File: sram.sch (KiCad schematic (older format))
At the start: 4 parts, among them U1 ICE40HX4K-TQ144, U2 IS61WV5128EDBLL-10TLI

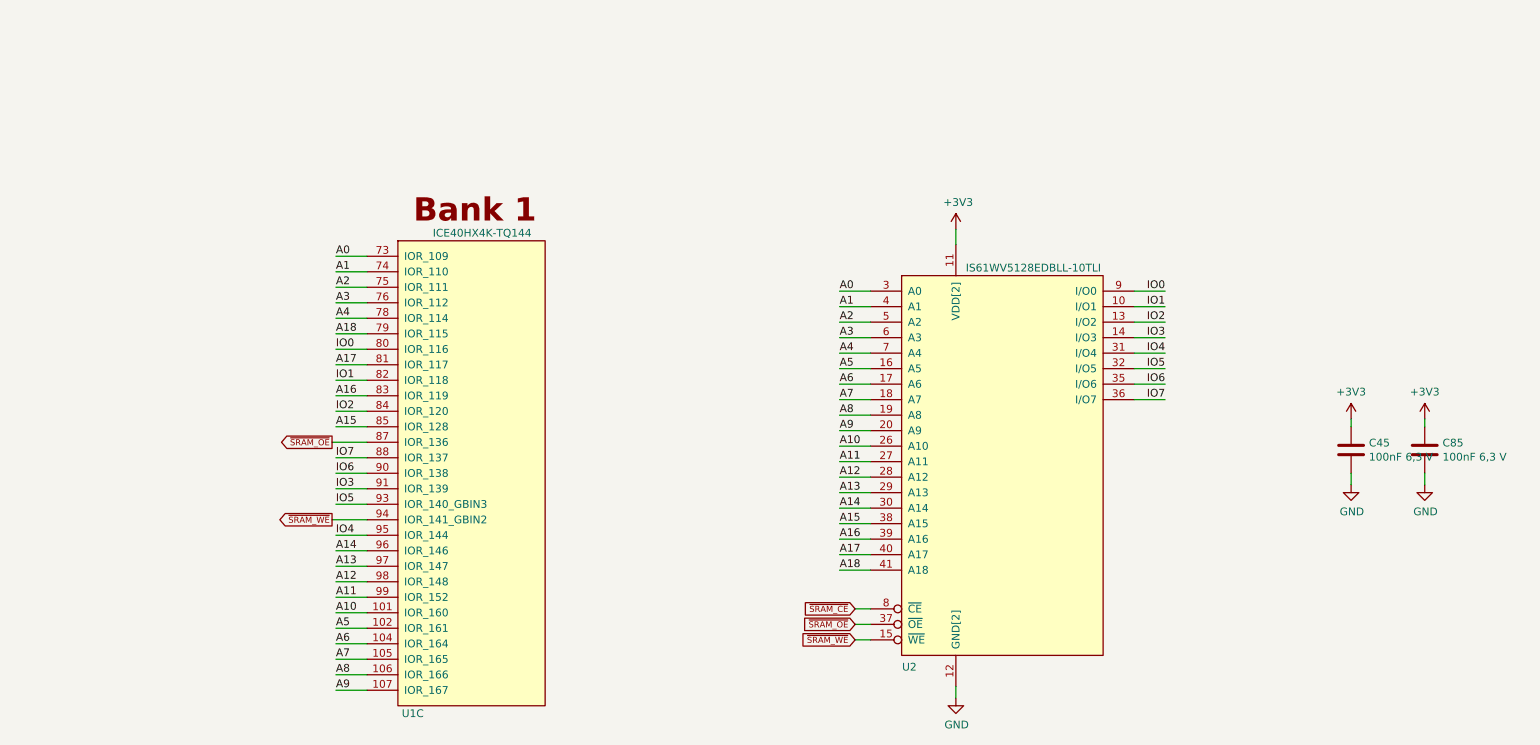
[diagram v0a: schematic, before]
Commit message: Schematic modified (Hierarchy) Bug where SPI was active when creset or ss was low fixed PCB layout started (almost all parts are at position) No parts on the bottom so far Arduino and PMOD header spacings corrected according to its standards
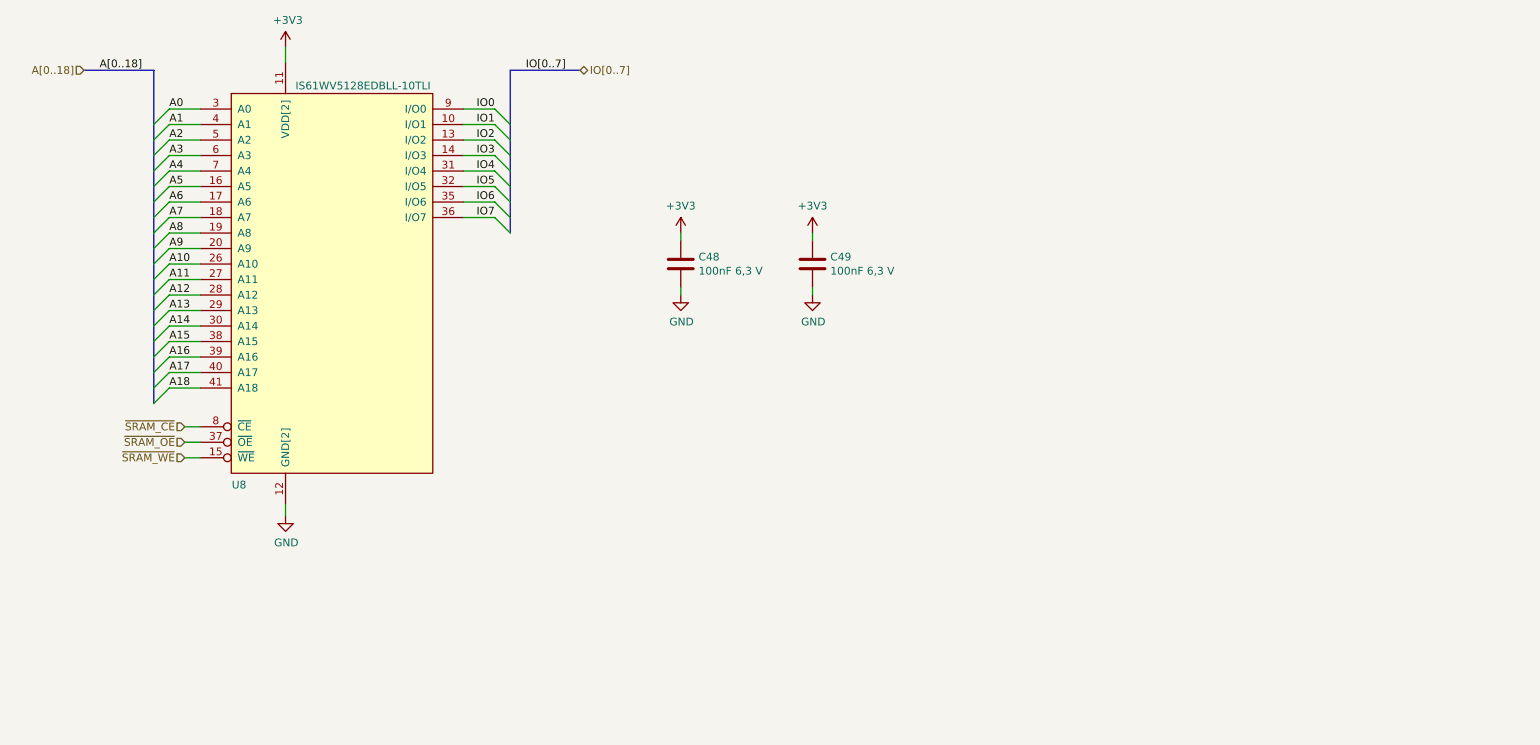
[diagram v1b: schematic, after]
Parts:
- removed U1: ICE40HX4K-TQ144, symbol ice40hx4k:ICE40HX4K-TQ144
- renumbered C45 to C48, C85 to C49, U2 to U8
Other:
- moved on the sheet: C48, C49, U8
